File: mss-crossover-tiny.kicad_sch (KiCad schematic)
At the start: 31 parts, among them J1 2x-screw, J2 RJ45, J3 2x-screw, J4 2x-screw, J5 ISP--5V, J6 TagConnect, J7 RJ45, SW1 Set, U1 L78M05CDT, U2 ACS724xLCTR-05AB, U3 ATtiny25-20SS, U4 AD8603, U5 LTV-355T

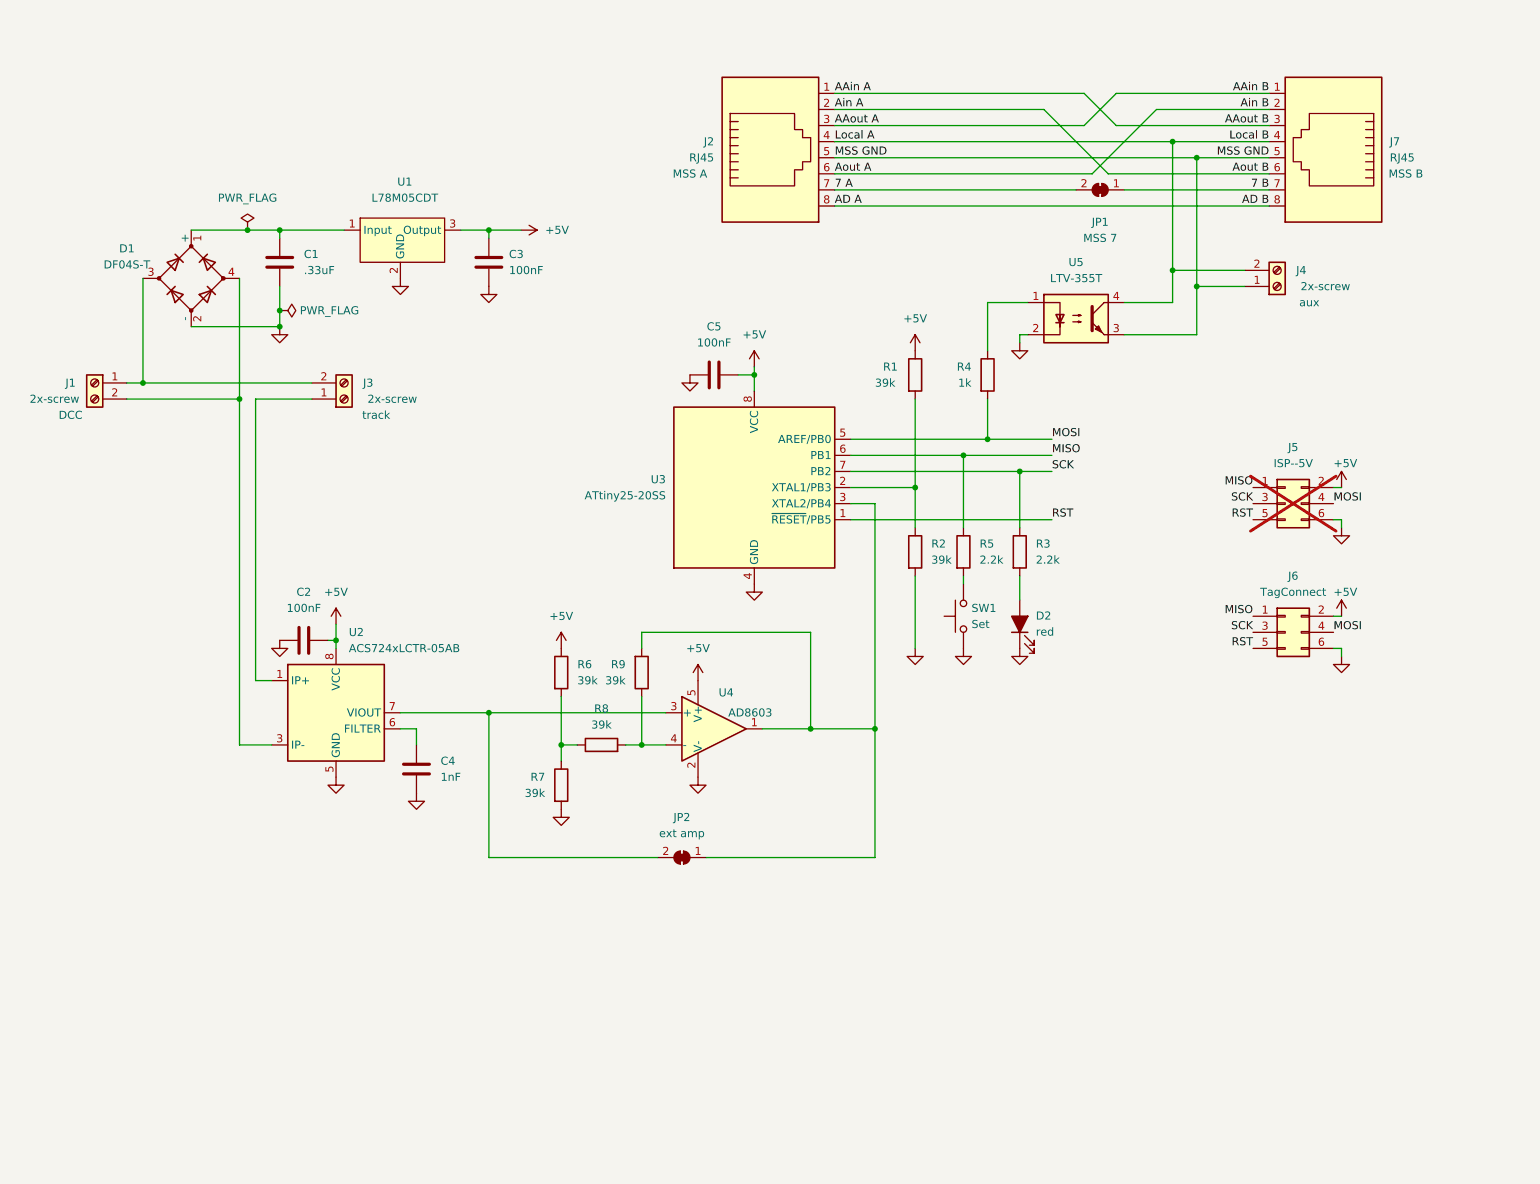
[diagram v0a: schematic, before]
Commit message: Added test points to board.  In src, added code to control the opto-isolator as well as the LED.
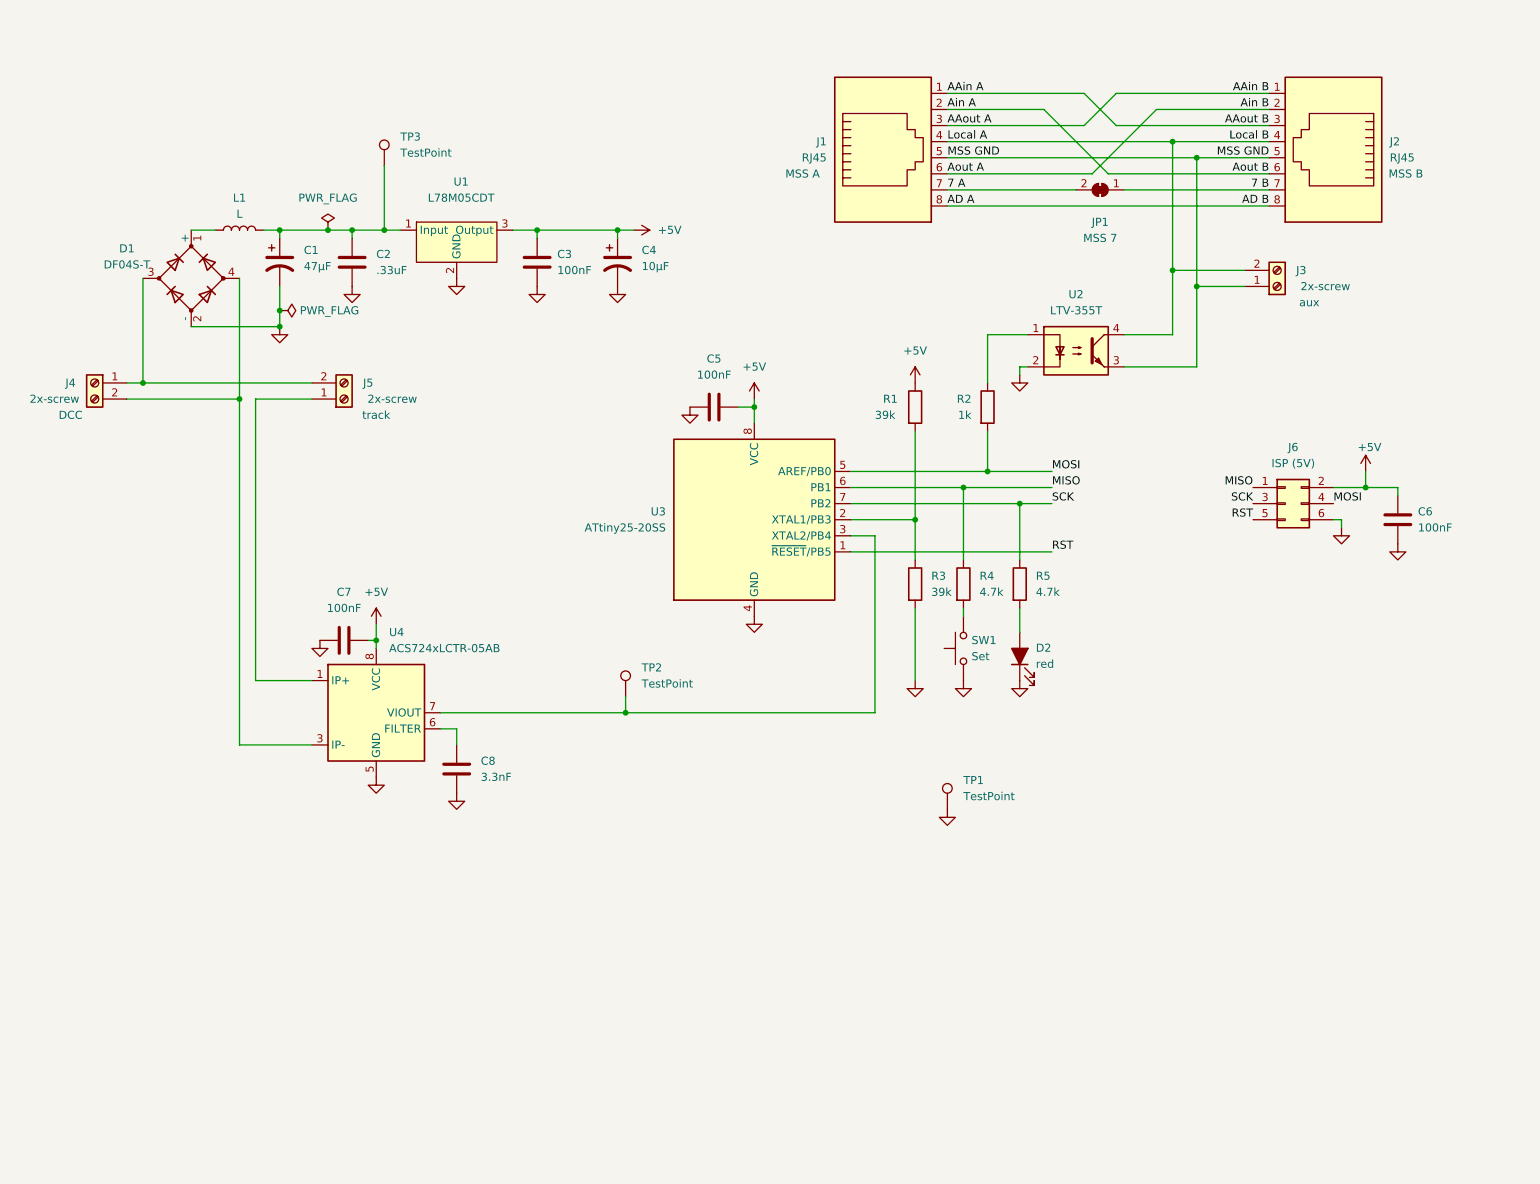
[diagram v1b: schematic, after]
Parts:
- removed J6: TagConnect, Connector:Tag-Connect_TC2030-IDC-NL_2x03_P1.27mm_Vertical, symbol Connector_Generic:Conn_02x03_Odd_Even
- removed JP2: ext amp, Jumper:SolderJumper-2_P1.3mm_Bridged_RoundedPad1.0x1.5mm, symbol Jumper:SolderJumper_2_Bridged
- removed R6, R7, R8, R9: 39k, Resistor_SMD:R_0805_2012Metric_Pad1.20x1.40mm_HandSolder, symbol Device:R
- removed U4: AD8603, Package_TO_SOT_SMD:TSOT-23-5, symbol Amplifier_Operational:AD8603
- added C1: 47µF, Capacitor_SMD:CP_Elec_6.3x5.7, symbol Device:C_Polarized_US
- added C4: 10µF, Capacitor_SMD:CP_Elec_4x5.7, symbol Device:C_Polarized_US
- added C6: 100nF, Capacitor_SMD:C_0805_2012Metric_Pad1.18x1.45mm_HandSolder, symbol Device:C
- added L1: L, Inductor_SMD:L_0805_2012Metric_Pad1.15x1.40mm_HandSolder, symbol Device:L
- added TP1, TP2, TP3: TestPoint, TestPoint:TestPoint_THTPad_1.5x1.5mm_Drill0.7mm, symbol Connector:TestPoint
- C8: renamed from C4; value 1nF -> 3.3nF; MPN CL21B102KBANNNC -> CL05B332KB5NNNC
- J6: renamed from J5; value ISP--5V -> ISP (5V); footprint myMods:PinHeader_2x03_P2.54mm_Vertical_Shrouded -> myMods:skedd-6-debugging; now fitted
- R4: renamed from R5; value 2.2k -> 4.7k; MPN RC0805FR-102K2L -> RC0805FR-104K7L
- R5: renamed from R3; value 2.2k -> 4.7k; MPN RC0805FR-102K2L -> RC0805FR-104K7L
- renumbered C1 to C2, C2 to C7, J2 to J1, J7 to J2, J4 to J3, J1 to J4, J3 to J5, R4 to R2, R2 to R3, U5 to U2, U2 to U4
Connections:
- net +5V: now also C4.1, C6.2
- net GND: now also C1.2, C4.2, C6.1, TP1.1
- net at C2.1, U1.1 (Input): now also C1.1, L1.2, TP3.1; no longer D1.1 (+)
- net at U4.7 (VIOUT): now also U3.3 (XTAL2/PB4), TP2.1
- new net: D1.1 (+), L1.1
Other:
- moved on the sheet: C2, C3, C5, C7, C8, D2, J1, R1, R2, R3, R4, R5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

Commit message: Updated some of the MPNs
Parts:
- U4: MPN ACS724LLCTR-05AB -> ACS724LLCTR-05AB-T
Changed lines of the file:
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@@
       (effects (font (size 1.27 1.27)) hide)
     )
-    (property "MPN" "ACS724LLCTR-05AB" (at 72.39 128.27 0)
+    (property "MPN" "ACS724LLCTR-05AB-T" (at 72.39 128.27 0)
       (effects (font (size 1.27 1.27)) hide)
     )

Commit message: Updated MPN for the ATtiny
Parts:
- U3: MPN ATtiny25-20SS -> ATtiny25-20SSU
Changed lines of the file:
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@@
       (effects (font (size 1.27 1.27)) hide)
     )
-    (property "MPN" "ATtiny25-20SS" (at 132.08 97.79 0)
+    (property "MPN" "ATtiny25-20SSU" (at 132.08 97.79 0)
       (effects (font (size 1.27 1.27)) hide)
     )

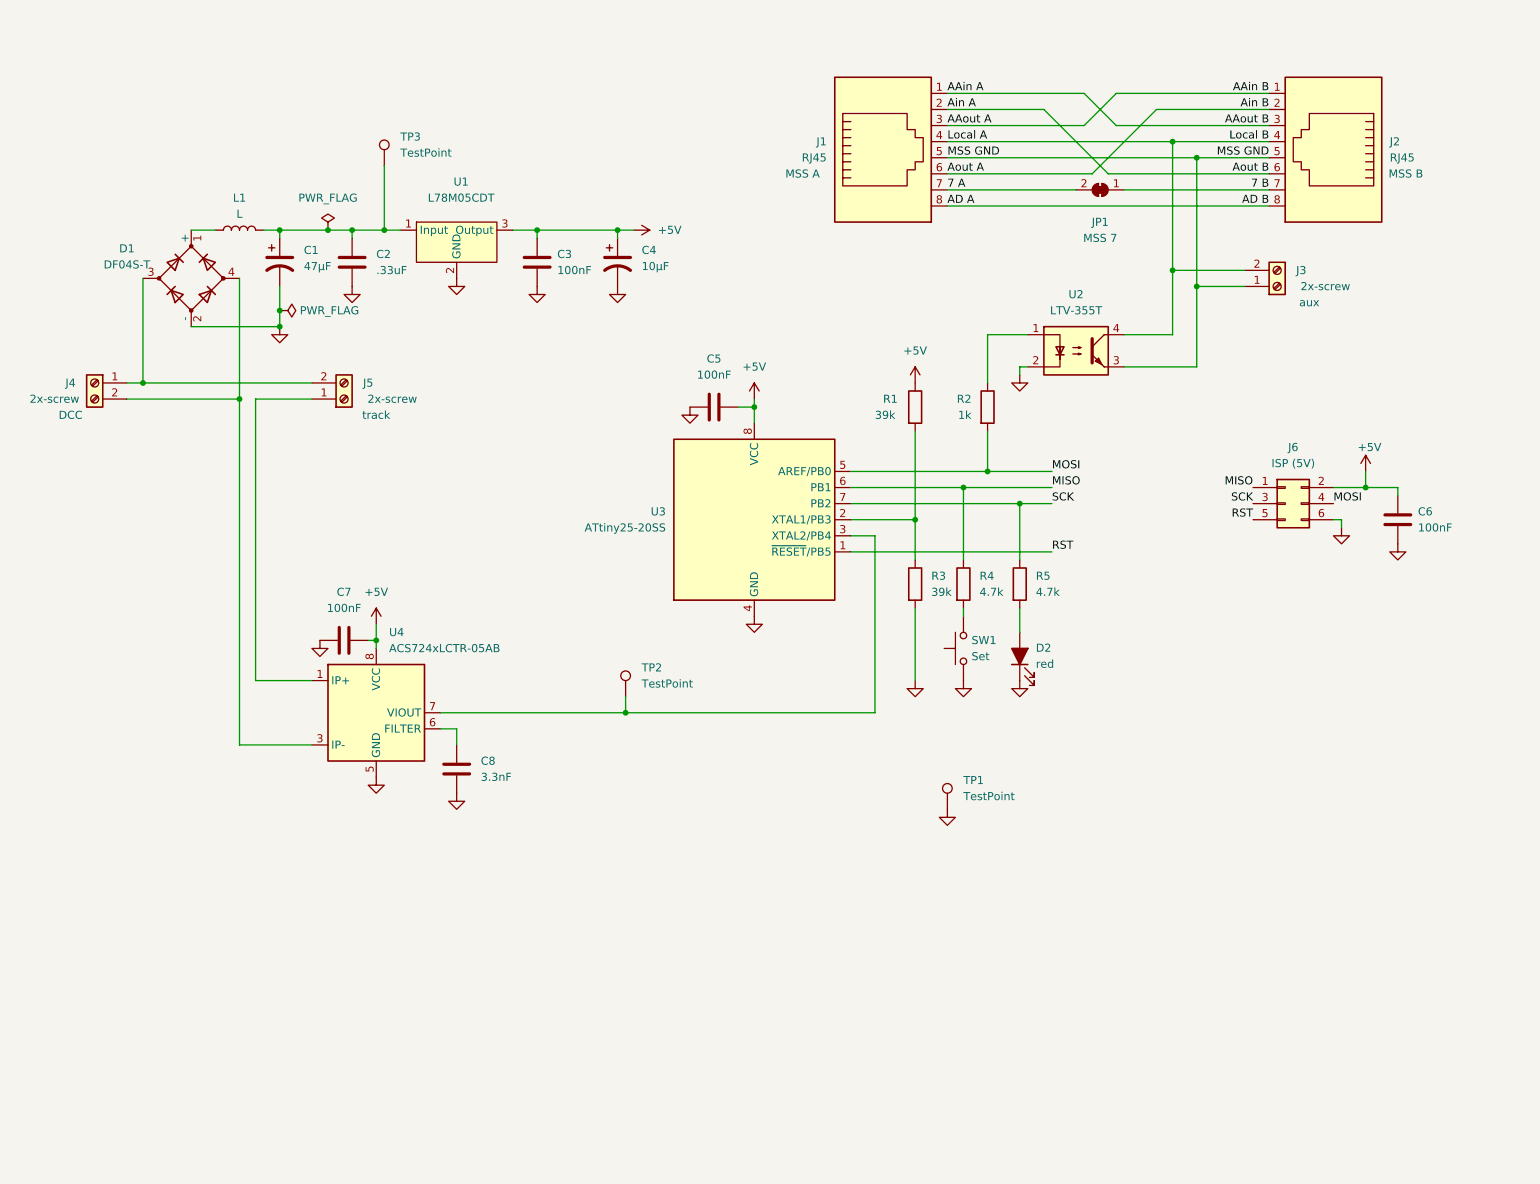
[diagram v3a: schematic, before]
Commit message: Changed to be able to plug the crossover board into a cascade board.
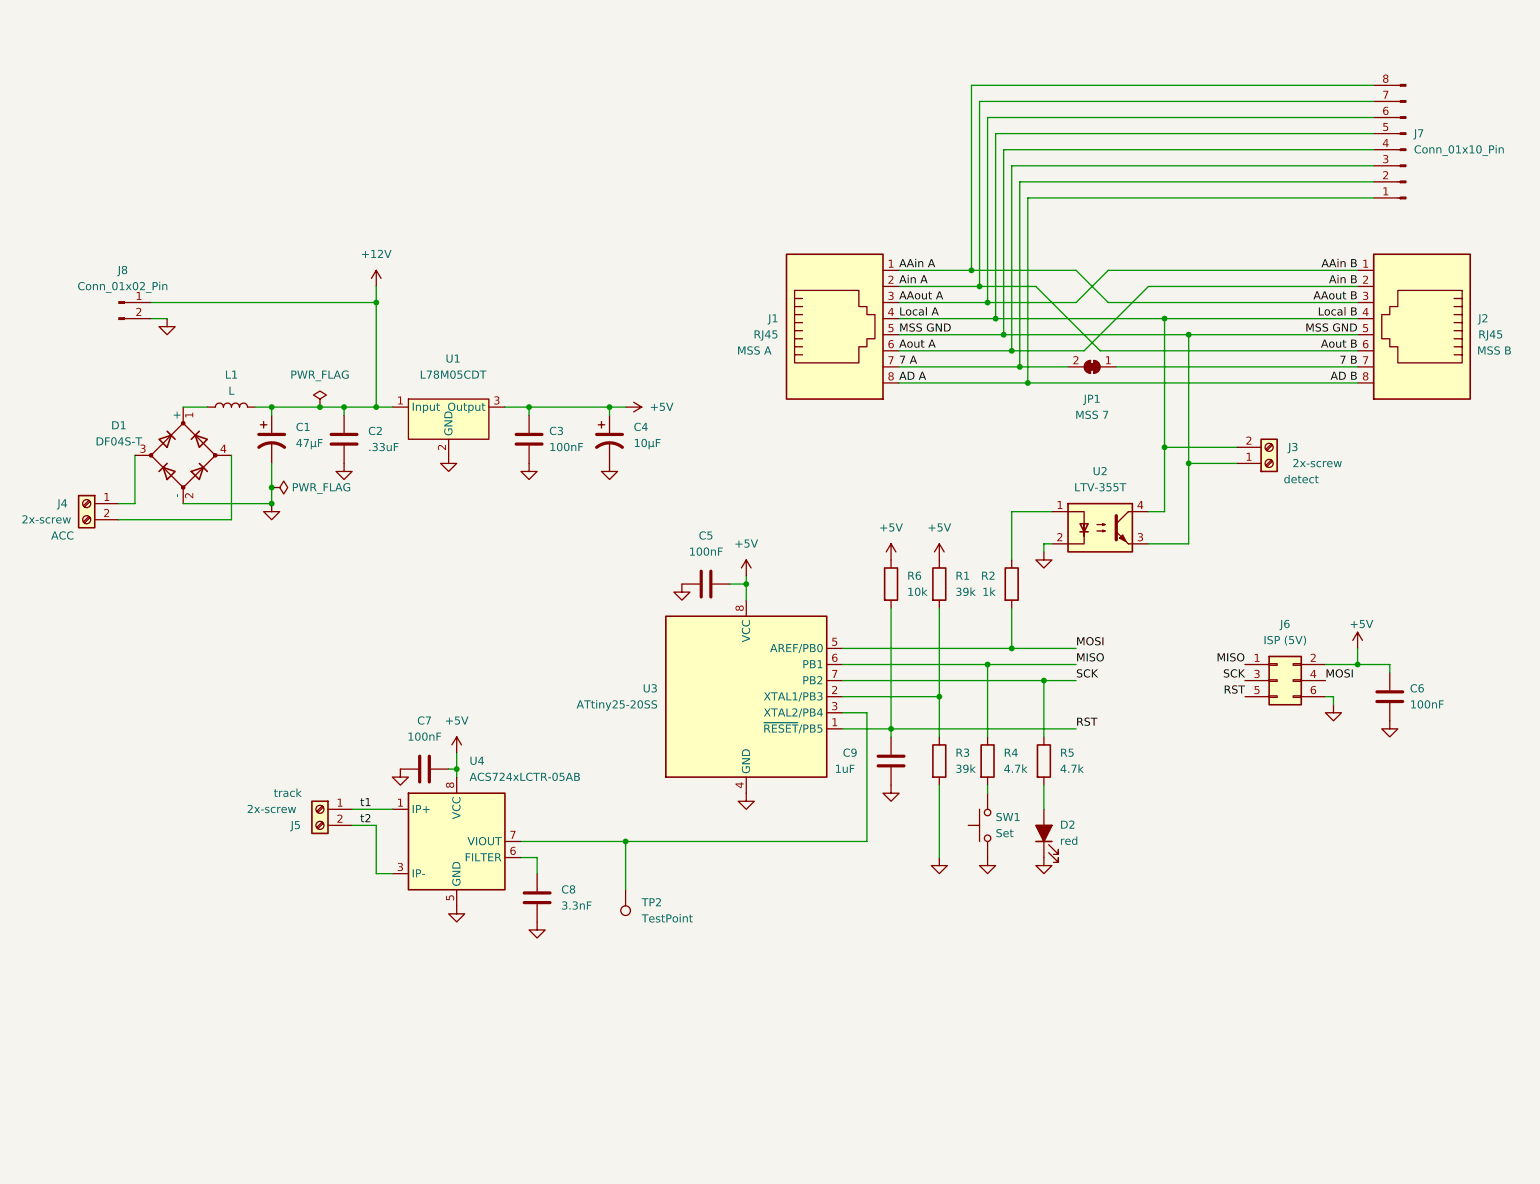
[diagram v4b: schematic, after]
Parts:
- removed TP1, TP3: TestPoint, TestPoint:TestPoint_THTPad_1.5x1.5mm_Drill0.7mm, symbol Connector:TestPoint
- added C9: 1uF, Capacitor_SMD:C_0805_2012Metric_Pad1.18x1.45mm_HandSolder, symbol Device:C
- added J7: Conn_01x10_Pin, Connector_PinHeader_2.00mm:PinHeader_1x08_P2.00mm_Vertical, symbol Connector:Conn_01x08_Pin
- added J8: Conn_01x02_Pin, Connector_PinHeader_2.00mm:PinHeader_1x02_P2.00mm_Vertical, symbol Connector:Conn_01x02_Pin
- added R6: 10k, Resistor_SMD:R_0805_2012Metric_Pad1.20x1.40mm_HandSolder, symbol Device:R
- J3: Label aux -> detect
- J4: Label DCC -> ACC
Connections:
- net +5V: now also R6.1
- net 7 A: now also J7.2 (Pin_2)
- net AAin A: now also J7.8 (Pin_8)
- net AAin B: now also J7.6 (Pin_6)
- net AD A: now also J7.1 (Pin_1)
- net Ain A: now also J7.7 (Pin_7)
- net Ain B: now also J7.3 (Pin_3)
- net GND: now also C9.1, J8.2 (Pin_2)
- net Local A: now also J7.5 (Pin_5)
- net MSS GND: now also J7.4 (Pin_4)
- net RST: now also C9.2, R6.2
- net at D1.3, J4.1 (Pin_1): no longer J5.2 (Pin_2)
- net at D1.4, J4.2 (Pin_2): no longer U4.3 (IP-), U4.4 (IP-)
- net t1: now reaches J5.1 (Pin_1), U4.1 (IP+), U4.2 (IP+)
- net +12V: now reaches C1.1, C2.1, L1.2, U1.1 (Input)
- net +12V: now also J8.1 (Pin_1)
- new net t2: J5.2 (Pin_2), U4.3 (IP-), U4.4 (IP-)
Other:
- moved on the sheet: C1, C2, C3, C4, C5, C6, C7, C8, D1, D2, J1, J2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
